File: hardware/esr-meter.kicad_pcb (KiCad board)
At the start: 2 copper layers, 66 x 99.1 mm, 105 parts, among them J1 USB_B_Micro, J2 JST-XH, J3 Pin Header Male, J4 Binding Post, Q1 DTC114E, Q2 IRLML6402, Q3 DTC114E, Q4 DTC114E, Q5 MMBFJ113, Q6 DTC114E, Q7 DTC114E, Q8 DTC114E, Q9 DTC114E, SW1 SW_Push, U1 MCP73831, U2 TPS60403, U3 TLV431, U4 OPA1678, U5 OPA1678, U6 ATmega88PA-AU, U7 QDSP-6064, U8 OPA1678

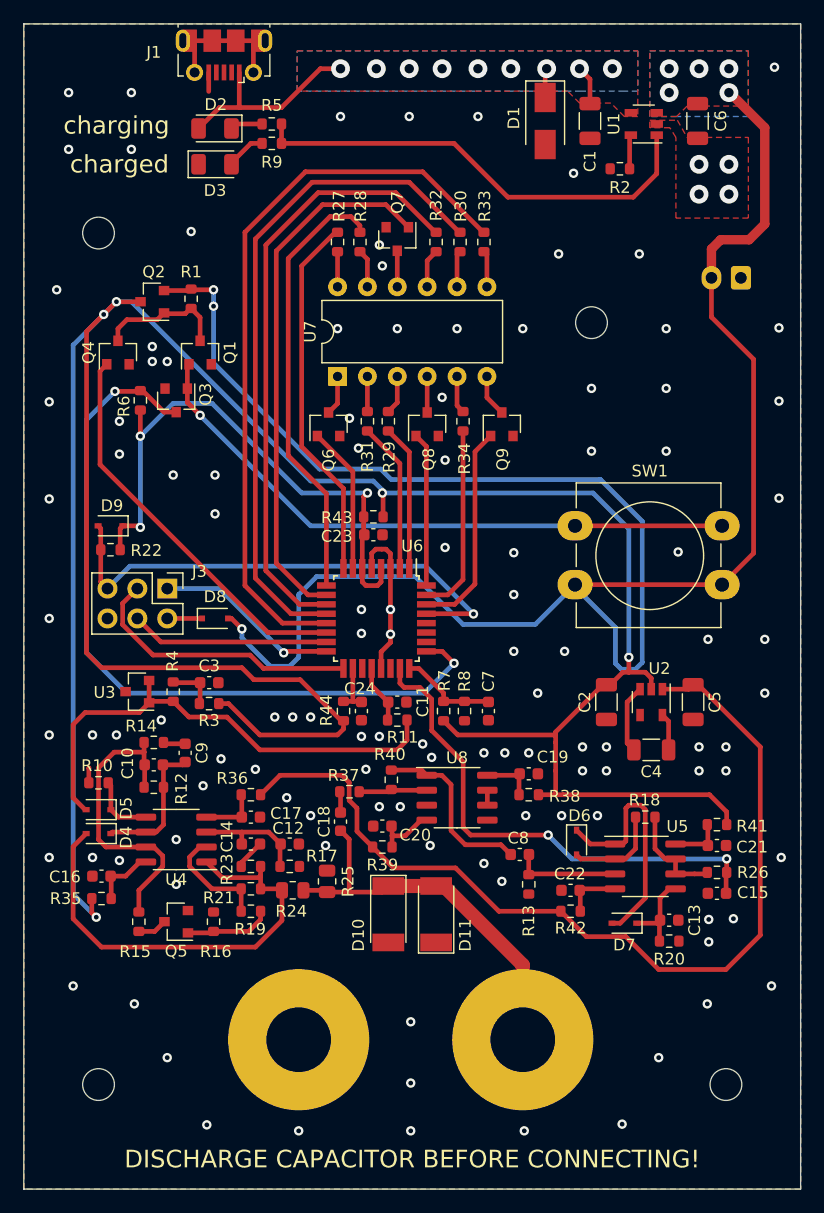
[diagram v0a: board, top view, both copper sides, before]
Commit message: Update to KiCad 7 and some minor changes
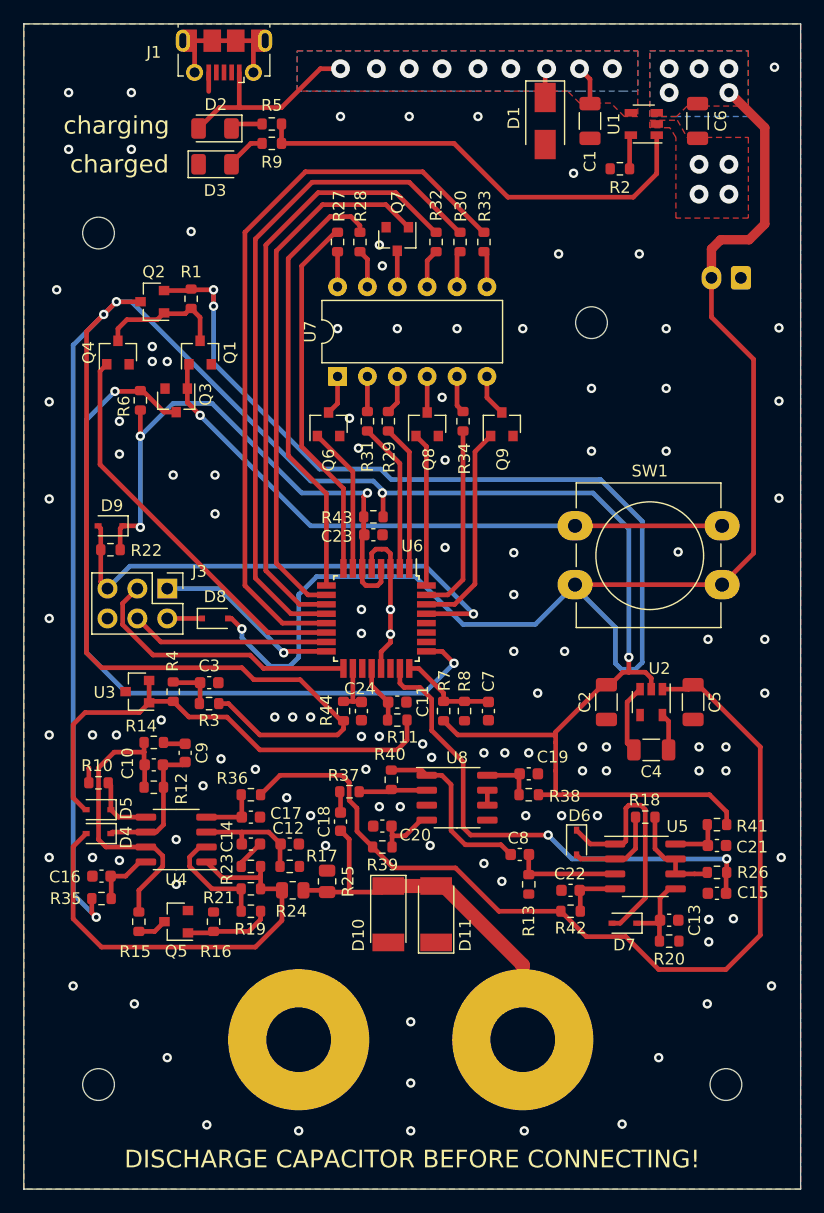
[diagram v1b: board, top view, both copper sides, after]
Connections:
- J1 pad 2: Net-(J1-Pad2) -> unconnected-(J1-D--Pad2)
- J1 pad 3: Net-(J1-Pad3) -> unconnected-(J1-D+-Pad3)
- J1 pad 4: Net-(J1-Pad4) -> unconnected-(J1-ID-Pad4)
- J1 pad 6: Net-(J1-Pad6) -> unconnected-(J1-Shield-Pad6)
- U6 pad 19: Net-(U6-Pad19) -> unconnected-(U6-ADC6-Pad19)
- U6 pad 22: Net-(U6-Pad22) -> unconnected-(U6-ADC7-Pad22)
- U6 pad 26: Net-(U6-Pad26) -> unconnected-(U6-PC3-Pad26)
- U6 pad 27: Net-(U6-Pad27) -> unconnected-(U6-PC4-Pad27)
- U6 pad 28: Net-(U6-Pad28) -> unconnected-(U6-PC5-Pad28)
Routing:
- net unconnected-(J1-Shield-Pad6): track 0.00 -> 11.5 mm
- net Net-(J1-Pad6): track 11.5 -> 0.00 mm
- net VBAT: track 177.9 -> 179.3 mm
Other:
- net class Default removed

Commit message: Split A2 circuit into A4 pages
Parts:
- C1, C6: value 4.7u -> 4.7μ
- C2, C4, C5: value 1u -> 1μ

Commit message: Change R11 to 100 ohm
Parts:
- R11: value 10 -> 100
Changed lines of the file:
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@@
         (effects (font (size 1 1) (thickness 0.15)))
     )
-    (fp_text value "10" (at 0 1.43) (layer "F.Fab")
+    (fp_text value "100" (at 0 1.43) (layer "F.Fab")
         (effects (font (size 1 1) (thickness 0.15)))
     )
